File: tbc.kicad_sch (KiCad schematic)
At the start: 0 parts

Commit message: major progress with memory interfacing
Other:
- sheet Frame Memories and Freeze ports: added FREEZE, Q1, Q2; removed none
- sheet Microcontroller, Power ports: added FREEZE; removed none
- sheet Video Encoder ports: added Q1, Q2; removed none

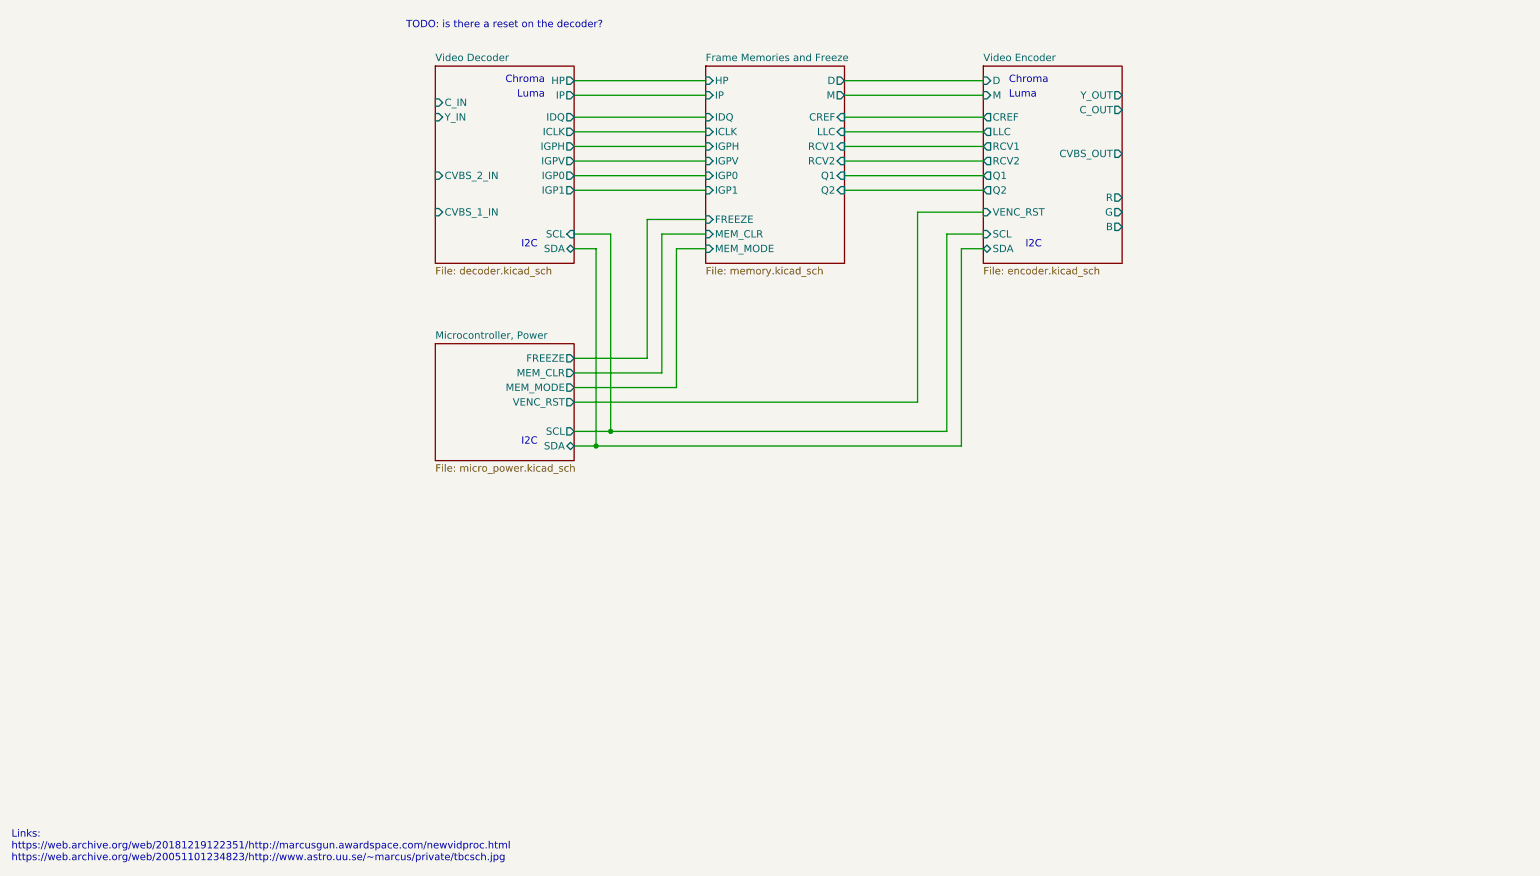
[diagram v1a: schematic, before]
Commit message: added connectors and crystal, osc
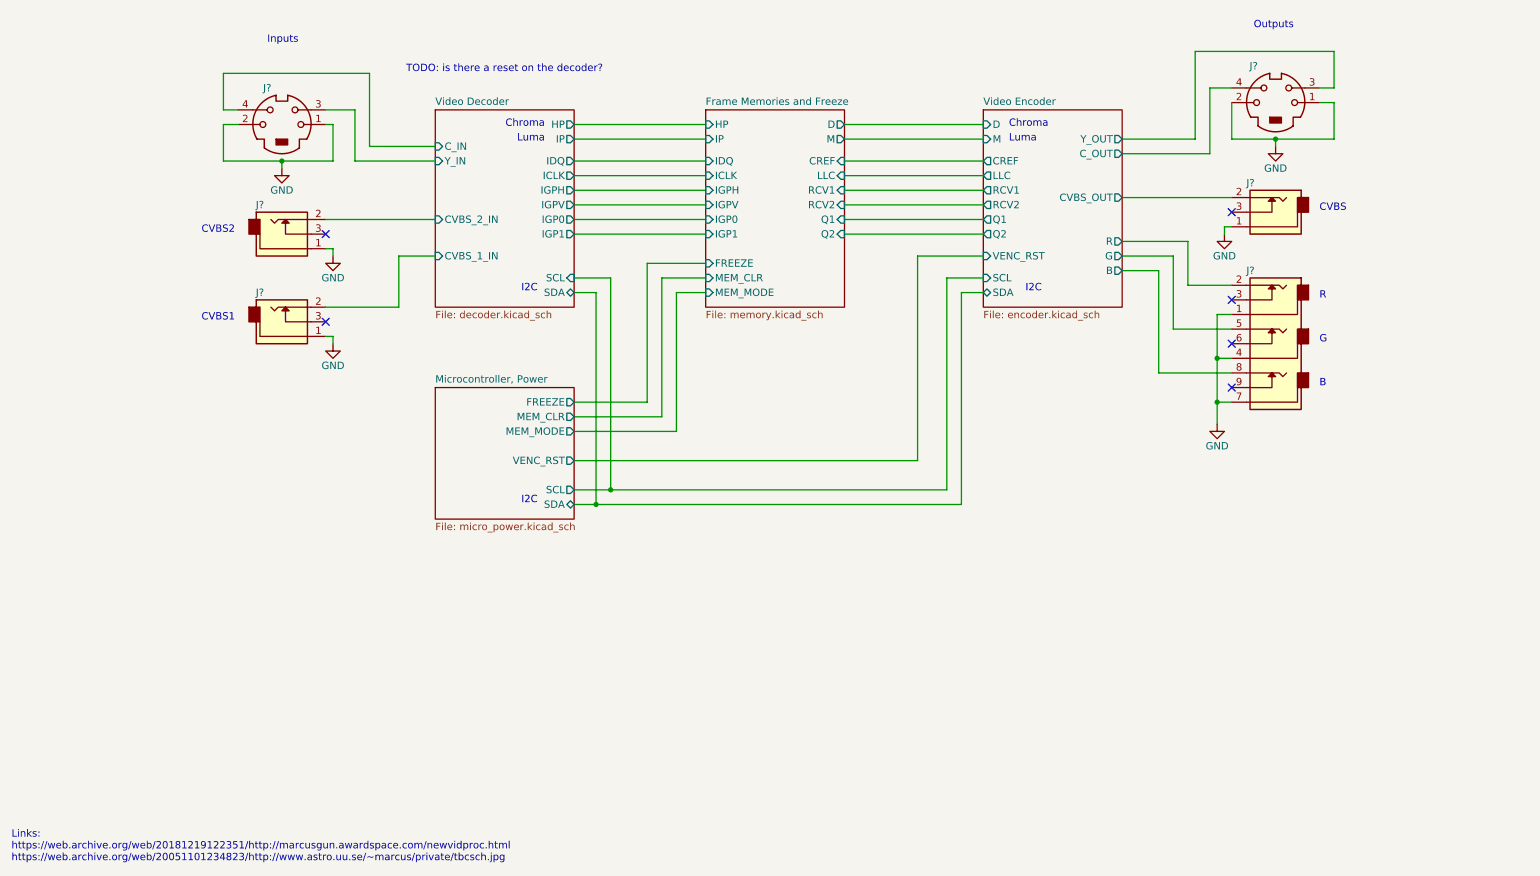
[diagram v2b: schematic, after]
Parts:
- added J? (x2): 5749181-1, symbol tbc:5749181-1
- added J? (x3): PJRAN1X1U01X, symbol tbc:PJRAN1X1U01X
- added J?: PJRAN3X1U03X, symbol tbc:PJRAN3X1U03X
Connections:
- net Video Decoder/CVBS_1_IN: now also J?.2
- net Video Decoder/CVBS_2_IN: now also J?.2
- net Video Decoder/C_IN: now also J?.4
- net Video Decoder/Y_IN: now also J?.3
- net Video Encoder/B: now also J?.8
- net Video Encoder/CVBS_OUT: now also J?.2
- net Video Encoder/C_OUT: now also J?.4
- net Video Encoder/G: now also J?.5
- net Video Encoder/R: now also J?.2
- net Video Encoder/Y_OUT: now also J?.3
- new net GND: J?.1, J?.1, J?.1, J?.1, J?.1, J?.1, J?.2, J?.2, J?.4, J?.7
- no-connect marks 0 -> 6
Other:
- note added: "B"
- note added: "CVBS"
- note added: "CVBS1"
- note added: "CVBS2"
- note added: "G"
- note added: "Inputs"
- note added: "Outputs"
- note added: "R"

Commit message: completed and annotated schematic, passed ERC
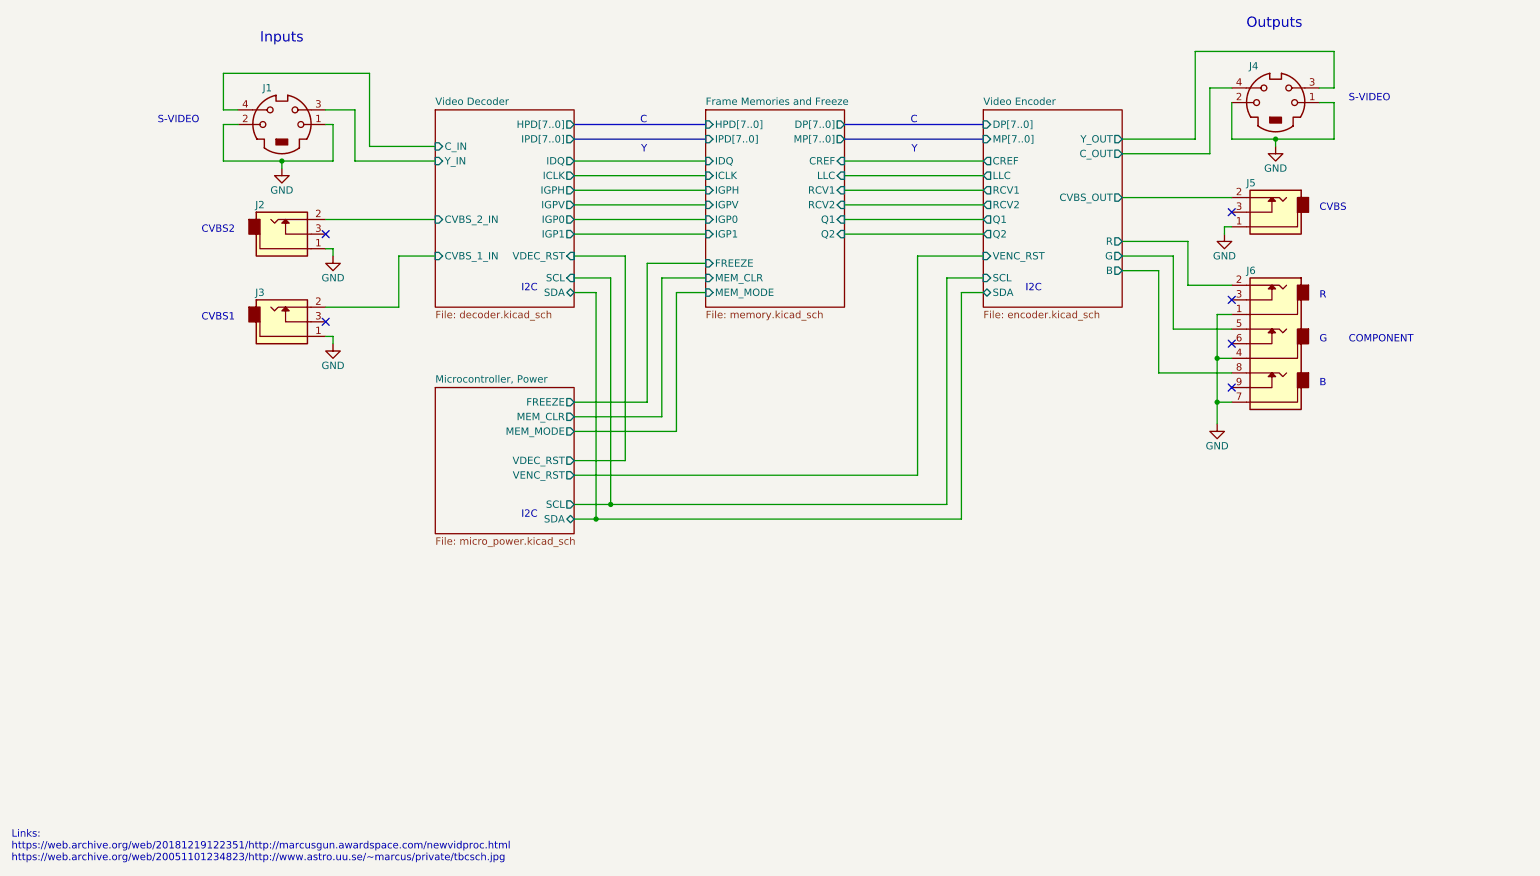
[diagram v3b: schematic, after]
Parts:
- gave numbers to parts that had none: 6
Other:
- sheet Frame Memories and Freeze ports: added DP[7..0], HPD[7..0], IPD[7..0], MP[7..0]; removed D, HP, IP, M
- sheet Microcontroller, Power ports: added VDEC_RST; removed none
- sheet Video Decoder ports: added HPD[7..0], IPD[7..0], VDEC_RST; removed HP, IP
- sheet Video Encoder ports: added DP[7..0], MP[7..0]; removed D, M
- note added: "C"
- note added: "COMPONENT"
- note added: "S-VIDEO"
- note added: "Y"
- note removed: "Chroma"
- note removed: "Luma"
- note removed: "TODO: is there a reset on the decoder?"

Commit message: connected shunt pins on switchcraft sockets correctly
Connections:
- net GND: now also J2.3, J3.3, J5.3, J6.3, J6.6, J6.9
- no-connect marks 6 -> 0
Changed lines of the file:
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@@
     (comment 4 "Original TBC circuit design © 2001 Marcus Gunnarsson (refer links on left)")
   )
+  (junction (at 226.06 111.76) (diameter 0) (color 0 0 0 0)
+  )
   (junction (at 118.11 134.62) (diameter 0) (color 0 0 0 0)
   )
+  (junction (at 72.39 87.63) (diameter 0) (color 0 0 0 0)
+  )
   (junction (at 236.22 68.58) (diameter 0) (color 0 0 0 0)
   )
@@
   (junction (at 63.5 72.39) (diameter 0) (color 0 0 0 0)
   )
+  (junction (at 226.06 104.14) (diameter 0) (color 0 0 0 0)
+  )
+  (junction (at 72.39 102.87) (diameter 0) (color 0 0 0 0)
+  )
   (junction (at 226.06 114.3) (diameter 0) (color 0 0 0 0)
   )
+  (junction (at 226.06 99.06) (diameter 0) (color 0 0 0 0)
+  )
   (junction (at 120.65 132.08) (diameter 0) (color 0 0 0 0)
   )
-  (no_connect (at 228.6 96.52))
-  (no_connect (at 71.12 85.09))
-  (no_connect (at 228.6 81.28))
-  (no_connect (at 228.6 111.76))
-  (no_connect (at 71.12 100.33))
-  (no_connect (at 228.6 104.14))
+  (junction (at 227.33 83.82) (diameter 0) (color 0 0 0 0)
+  )
   (wire (pts (xy 209.55 68.58) (xy 222.25 68.58))
     (stroke (width 0) (type default))
@@
     (stroke (width 0) (type default))
   )
+  (wire (pts (xy 72.39 100.33) (xy 72.39 102.87))
+    (stroke (width 0) (type default))
+  )
   (wire (pts (xy 161.29 80.01) (xy 185.42 80.01))
     (stroke (width 0) (type default))
@@
     (stroke (width 0) (type default))
   )
-  (wire (pts (xy 226.06 99.06) (xy 226.06 106.68))
+  (wire (pts (xy 226.06 99.06) (xy 226.06 104.14))
     (stroke (width 0) (type default))
   )
@@
     (stroke (width 0) (type default))
   )
+  (wire (pts (xy 226.06 104.14) (xy 228.6 104.14))
+    (stroke (width 0) (type default))
+  )
   (wire (pts (xy 114.3 77.47) (xy 137.16 77.47))
     (stroke (width 0) (type default))
@@
     (stroke (width 0) (type default))
   )
+  (wire (pts (xy 226.06 104.14) (xy 226.06 106.68))
+    (stroke (width 0) (type default))
+  )
   (wire (pts (xy 224.79 59.69) (xy 228.6 59.69))
     (stroke (width 0) (type default))
@@
     (stroke (width 0) (type default))
   )
+  (wire (pts (xy 226.06 111.76) (xy 228.6 111.76))
+    (stroke (width 0) (type default))
+  )
   (wire (pts (xy 227.33 83.82) (xy 227.33 85.09))
     (stroke (width 0) (type default))
   )
+  (wire (pts (xy 227.33 81.28) (xy 227.33 83.82))
+    (stroke (width 0) (type default))
+  )
+  (wire (pts (xy 228.6 96.52) (xy 226.06 96.52))
+    (stroke (width 0) (type default))
+  )
   (wire (pts (xy 218.44 101.6) (xy 228.6 101.6))
     (stroke (width 0) (type default))
   )
-  (wire (pts (xy 226.06 106.68) (xy 226.06 114.3))
+  (wire (pts (xy 226.06 106.68) (xy 226.06 111.76))
     (stroke (width 0) (type default))
   )
@@
     (stroke (width 0) (type default))
   )
+  (wire (pts (xy 71.12 100.33) (xy 72.39 100.33))
+    (stroke (width 0) (type default))
+  )
   (wire (pts (xy 114.3 127) (xy 173.99 127))
     (stroke (width 0) (type default))
   )
+  (wire (pts (xy 71.12 85.09) (xy 72.39 85.09))
+    (stroke (width 0) (type default))
+  )
   (wire (pts (xy 114.3 124.46) (xy 123.19 124.46))
     (stroke (width 0) (type default))
@@
     (stroke (width 0) (type default))
   )
+  (wire (pts (xy 228.6 81.28) (xy 227.33 81.28))
+    (stroke (width 0) (type default))
+  )
   (wire (pts (xy 132.08 119.38) (xy 132.08 95.25))
     (stroke (width 0) (type default))
@@
     (stroke (width 0) (type default))
   )
+  (wire (pts (xy 226.06 111.76) (xy 226.06 114.3))
+    (stroke (width 0) (type default))
+  )
   (wire (pts (xy 78.74 69.85) (xy 78.74 57.15))
     (stroke (width 0) (type default))
@@
     (stroke (width 0) (type default))
   )
+  (wire (pts (xy 72.39 85.09) (xy 72.39 87.63))
+    (stroke (width 0) (type default))
+  )
   (wire (pts (xy 161.29 77.47) (xy 185.42 77.47))
     (stroke (width 0) (type default))
   )
+  (wire (pts (xy 226.06 96.52) (xy 226.06 99.06))
+    (stroke (width 0) (type default))
+  )

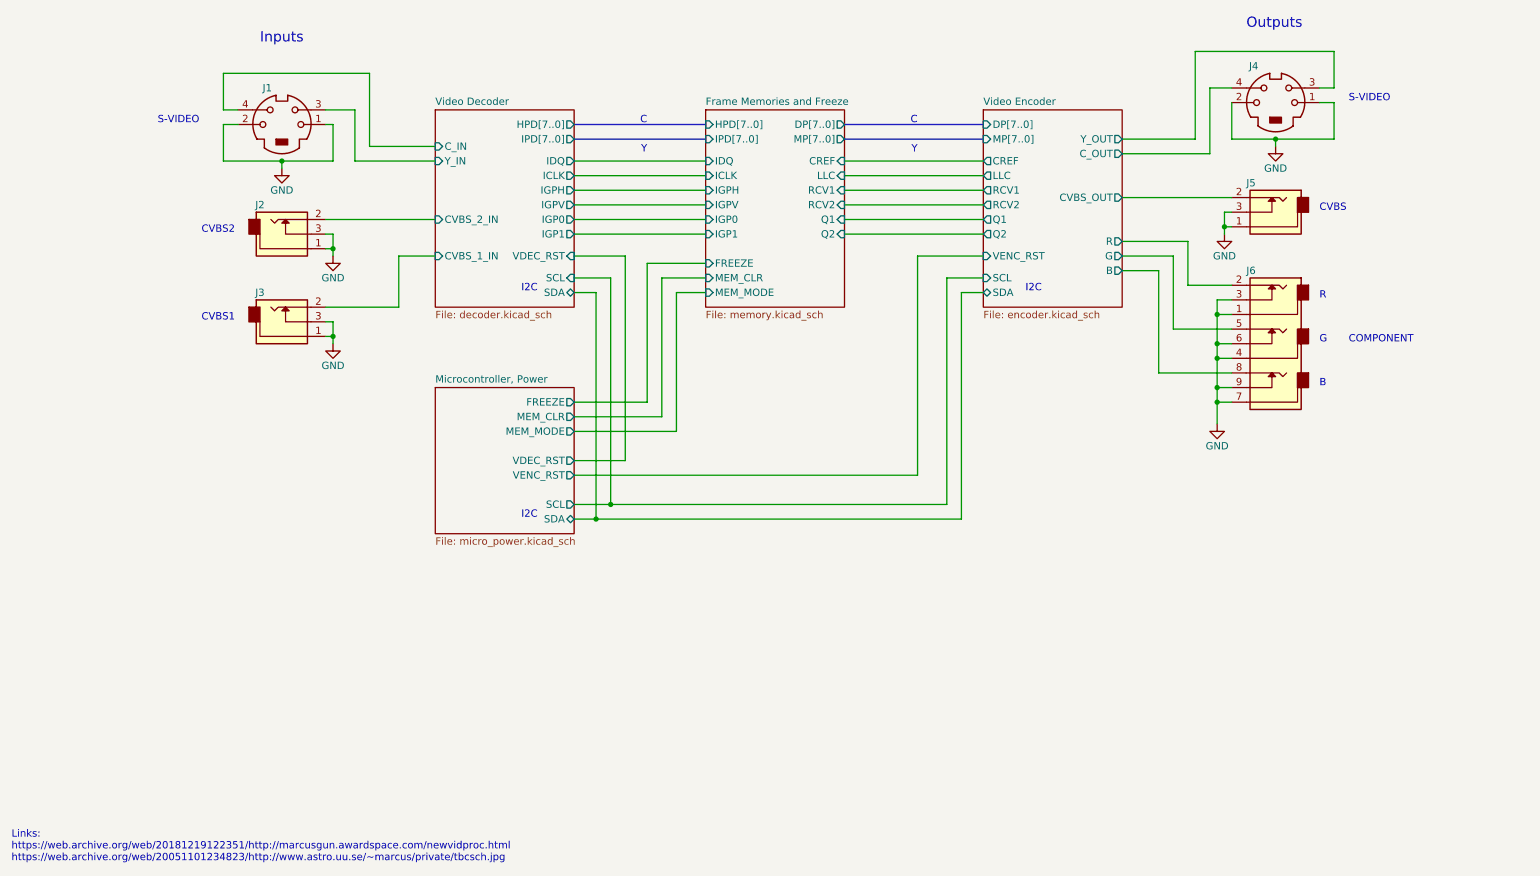
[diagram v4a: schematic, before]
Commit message: added notes, schematic cleanup
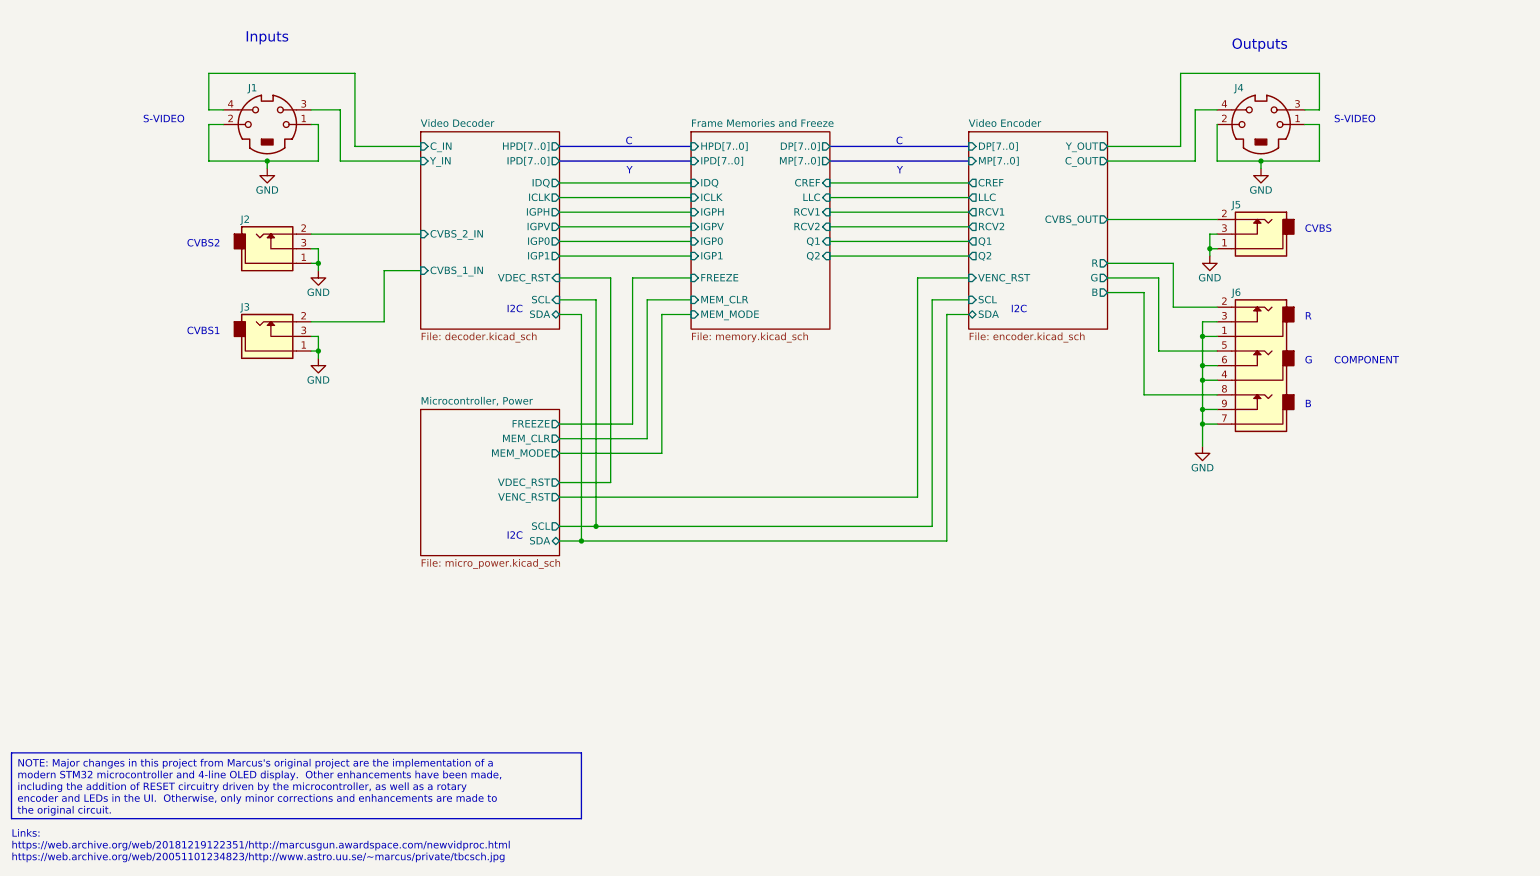
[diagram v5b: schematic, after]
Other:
- moved on the sheet: J1, J2, J3, J4, J5, J6

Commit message: minor cleanup, addition of notes
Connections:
- net GND: no longer J5.3, J6.3, J6.6, J6.9
- no-connect marks 0 -> 4
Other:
- note removed: "Links: https://web.archive.org/web/20181219122351/http://marcusgun.awardspace.com/newvidproc.html https://web.archive.org/web/20051101234823/http://www.astro.uu.se/~marcus/private/tbcsch.jpg"
- moved on the sheet: J1, J2, J3, J4, J5, J6

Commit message: added connector footprints
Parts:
- J1, J4: footprint (none) -> tbc:5749181-1
- J2, J3, J5: footprint (none) -> tbc:PJRAN1X1U01X
- J6: footprint (none) -> tbc:PJRAN3X1U03X
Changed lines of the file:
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@@
       (effects (font (size 1.27 1.27)) hide)
     )
-    (property "Footprint" "" (at 219.71 64.77 0)
+    (property "Footprint" "tbc:5749181-1" (at 219.71 64.77 0)
       (effects (font (size 1.27 1.27)) hide)
     )
@@
       (effects (font (size 1.27 1.27)) hide)
     )
-    (property "Footprint" "" (at 49.53 104.14 0)
+    (property "Footprint" "tbc:PJRAN1X1U01X" (at 49.53 104.14 0)
       (effects (font (size 1.27 1.27)) hide)
     )
@@
       (effects (font (size 1.27 1.27)) (justify right) hide)
     )
-    (property "Footprint" "" (at 217.17 86.36 0)
+    (property "Footprint" "tbc:PJRAN1X1U01X" (at 217.17 86.36 0)
       (effects (font (size 1.27 1.27)) hide)
     )
@@
       (effects (font (size 1.27 1.27)) hide)
     )
-    (property "Footprint" "" (at 49.53 87.63 0)
+    (property "Footprint" "tbc:PJRAN1X1U01X" (at 49.53 87.63 0)
       (effects (font (size 1.27 1.27)) hide)
     )
@@
       (effects (font (size 1.27 1.27)) (justify right) hide)
     )
-    (property "Footprint" "" (at 217.17 101.6 0)
+    (property "Footprint" "tbc:PJRAN3X1U03X" (at 217.17 101.6 0)
       (effects (font (size 1.27 1.27)) hide)
     )
@@
       (effects (font (size 1.27 1.27)) hide)
     )
-    (property "Footprint" "" (at 46.99 64.77 0)
+    (property "Footprint" "tbc:5749181-1" (at 46.99 64.77 0)
       (effects (font (size 1.27 1.27)) hide)
     )
